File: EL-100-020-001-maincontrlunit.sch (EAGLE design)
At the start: 186 parts, among them T1 WS-TST-90°, U1 VNI4140K-32, U16 24AA256-I/SN, U19 ABS10-32.768KHZ-7-T, U2 VNI4140K-32, U3 VNI4140K-32, U8 MCP7940N-I/SN, U9 PMEG2005ET, X1 944-12-46-00, X10 S2L3.50/8/90G, X11 S2L3.50/8/90G, X12 S2L3.50/8/90G, X13 140-08-FLACHBAND1.27, X14 944-12-2-00, X2 944-12-46-00, X3 90G-14, X4 90G-14, X5 Q-063209, X6 Q-063209, X7 Q-063209, X8 Q-063209, X9 S2L3.50/8/90G

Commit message: extensions added
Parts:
- added C65: 1000pF, supply2:C1206C102KDRACTU
- C39, C40: value 4.7nF -> 4700pF
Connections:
- net AGND: now also C65.C1
- net PE: now also C65.C2
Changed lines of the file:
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@@
 </part>
 <part name="SUPPLY53" library="supply2" deviceset="PE" device=""/>
-<part name="C39" library="Kemet_By_element14_1" deviceset="C0805F472K1RACAUTO" device="" value="4.7nF"/>
-<part name="C40" library="Kemet_By_element14_1" deviceset="C0805F472K1RACAUTO" device="" value="4.7nF"/>
+<part name="C39" library="Kemet_By_element14_1" deviceset="C0805F472K1RACAUTO" device="" value="4700pF"/>
+<part name="C40" library="Kemet_By_element14_1" deviceset="C0805F472K1RACAUTO" device="" value="4700pF"/>
 <part name="SUPPLY54" library="supply2" deviceset="0V" device=""/>
 <part name="C1" library="Kemet_By_element14_1" deviceset="C1206C225K5RACTU" device="" value="2.2uF"/>
@@
 <attribute name="MF" value="VISHAY DRALORIC"/>
 </part>
+<part name="C65" library="supply2" deviceset="C1206C102KDRACTU" device="" value="1000pF">
+<attribute name="MF" value="KEMET"/>
+<attribute name="OC_FARNELL" value="1826304"/>
+</part>
+<part name="SUPPLY108" library="supply2" deviceset="AGND" device=""/>
+<part name="SUPPLY109" library="supply2" deviceset="PE" device=""/>
 </parts>
 <sheets>
@@
 <instance part="SUPPLY77" gate="PE" x="322.58" y="185.42"/>
 <instance part="SUPPLY79" gate="PE" x="322.58" y="208.28"/>
+<instance part="C65" gate="G$1" x="195.58" y="241.3" smashed="yes">
+<attribute name="VALUE" x="189.9158" y="237.0328" size="1.778" layer="96" ratio="10" rot="SR0"/>
+<attribute name="NAME" x="194.6656" y="244.0686" size="2.0828" layer="95" ratio="10" rot="SR0"/>
+<attribute name="MF" x="195.58" y="241.3" size="1.778" layer="96" rot="R270" display="off"/>
+</instance>
+<instance part="SUPPLY108" gate="G$1" x="182.88" y="236.22" rot="MR0"/>
+<instance part="SUPPLY109" gate="PE" x="213.36" y="236.22"/>
 </instances>
 <busses>
@@
 <pinref part="SUPPLY105" gate="G$1" pin="AGND"/>
 </segment>
+<segment>
+<pinref part="C65" gate="G$1" pin="C1"/>
+<pinref part="SUPPLY108" gate="G$1" pin="AGND"/>
+<wire x1="195.58" y1="241.3" x2="182.88" y2="241.3" width="0.1524" layer="91"/>
+<wire x1="182.88" y1="241.3" x2="182.88" y2="238.76" width="0.1524" layer="91"/>
+</segment>
 </net>
 <net name="ANA_1.1" class="0">
@@
 <pinref part="SUPPLY79" gate="PE" pin="PE"/>
 </segment>
+<segment>
+<pinref part="C65" gate="G$1" pin="C2"/>
+<pinref part="SUPPLY109" gate="PE" pin="PE"/>
+<wire x1="203.2" y1="241.3" x2="213.36" y2="241.3" width="0.1524" layer="91"/>
+<wire x1="213.36" y1="241.3" x2="213.36" y2="238.76" width="0.1524" layer="91"/>
+</segment>
 </net>

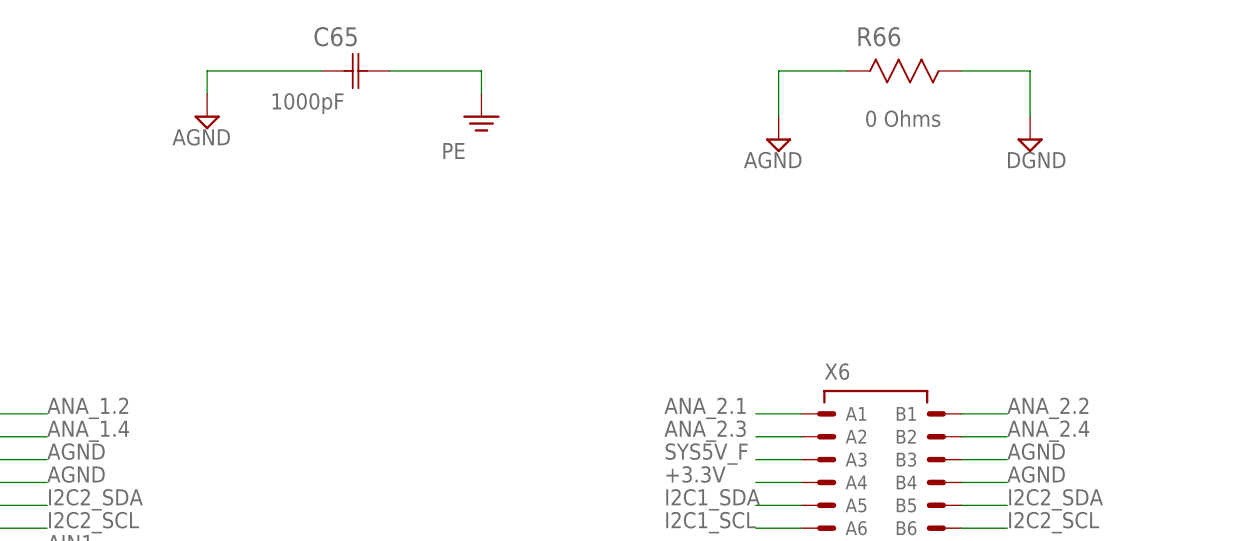
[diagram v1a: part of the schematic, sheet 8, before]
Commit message: DIN Rail extension
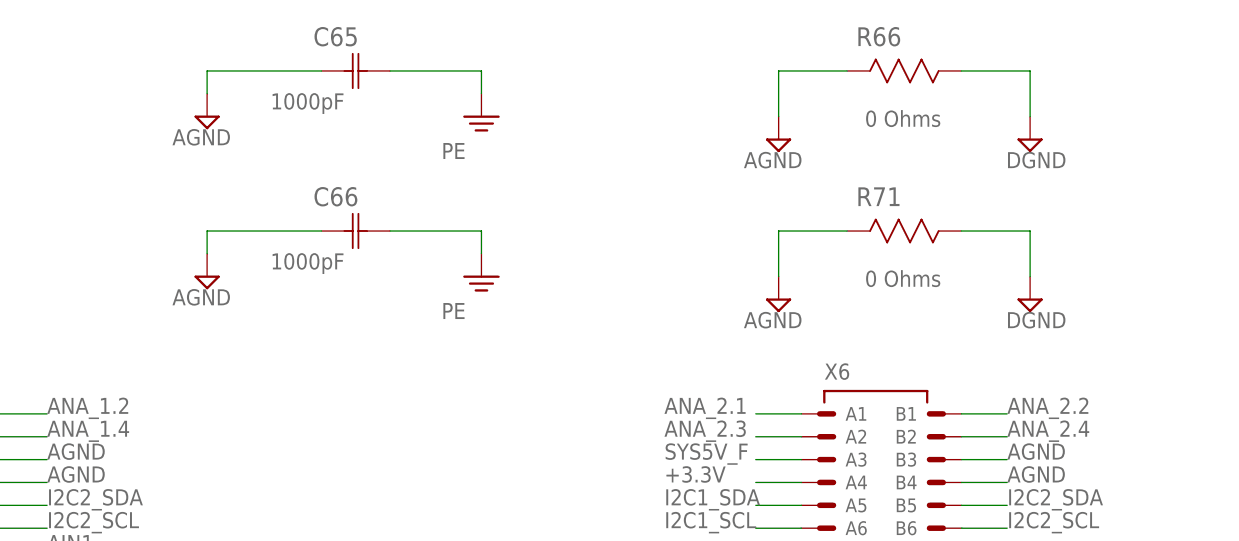
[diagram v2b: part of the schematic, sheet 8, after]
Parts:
- added C66: 1000pF, supply2:C1206C102KDRACTU
- added R71: 0 Ohms, Vishay_By_element14_Batch_1:CRCW12060000Z0EA
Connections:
- net AGND: now also C66.C1, R71.2
- net DGND: now also R71.1
- net PE: now also C66.C2
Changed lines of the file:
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@@
 <part name="SUPPLY108" library="supply2" deviceset="AGND" device=""/>
 <part name="SUPPLY109" library="supply2" deviceset="PE" device=""/>
+<part name="R71" library="Vishay_By_element14_Batch_1" deviceset="CRCW12060000Z0EA" device="" value="0 Ohms"/>
+<part name="SUPPLY110" library="supply2" deviceset="AGND" device=""/>
+<part name="SUPPLY111" library="supply2" deviceset="DGND" device=""/>
+<part name="C66" library="supply2" deviceset="C1206C102KDRACTU" device="" value="1000pF">
+<attribute name="MF" value="KEMET"/>
+<attribute name="OC_FARNELL" value="1826304"/>
+</part>
+<part name="SUPPLY112" library="supply2" deviceset="AGND" device=""/>
+<part name="SUPPLY113" library="supply2" deviceset="PE" device=""/>
 </parts>
 <sheets>
@@
 <instance part="SUPPLY108" gate="G$1" x="182.88" y="236.22" rot="MR0"/>
 <instance part="SUPPLY109" gate="PE" x="213.36" y="236.22"/>
+<instance part="R71" gate="A" x="254" y="223.52" smashed="yes">
+<attribute name="VALUE" x="255.9558" y="217.3224" size="1.778" layer="96" ratio="10" rot="SR0"/>
+<attribute name="NAME" x="254.9906" y="226.2886" size="2.0828" layer="95" ratio="10" rot="SR0"/>
+</instance>
+<instance part="SUPPLY110" gate="G$1" x="246.38" y="215.9" rot="MR0"/>
+<instance part="SUPPLY111" gate="G$1" x="274.32" y="215.9"/>
+<instance part="C66" gate="G$1" x="195.58" y="223.52" smashed="yes">
+<attribute name="VALUE" x="189.9158" y="219.2528" size="1.778" layer="96" ratio="10" rot="SR0"/>
+<attribute name="NAME" x="194.6656" y="226.2886" size="2.0828" layer="95" ratio="10" rot="SR0"/>
+<attribute name="MF" x="195.58" y="223.52" size="1.778" layer="96" rot="R270" display="off"/>
+</instance>
+<instance part="SUPPLY112" gate="G$1" x="182.88" y="218.44" rot="MR0"/>
+<instance part="SUPPLY113" gate="PE" x="213.36" y="218.44"/>
 </instances>
 <busses>
@@
 <wire x1="182.88" y1="241.3" x2="182.88" y2="238.76" width="0.1524" layer="91"/>
 </segment>
+<segment>
+<wire x1="254" y1="223.52" x2="246.38" y2="223.52" width="0.1524" layer="91"/>
+<wire x1="246.38" y1="223.52" x2="246.38" y2="218.44" width="0.1524" layer="91"/>
+<pinref part="R71" gate="A" pin="2"/>
+<pinref part="SUPPLY110" gate="G$1" pin="AGND"/>
+</segment>
+<segment>
+<pinref part="C66" gate="G$1" pin="C1"/>
+<pinref part="SUPPLY112" gate="G$1" pin="AGND"/>
+<wire x1="195.58" y1="223.52" x2="182.88" y2="223.52" width="0.1524" layer="91"/>
+<wire x1="182.88" y1="223.52" x2="182.88" y2="220.98" width="0.1524" layer="91"/>
+</segment>
 </net>
 <net name="ANA_1.1" class="0">
@@
 <wire x1="266.7" y1="241.3" x2="274.32" y2="241.3" width="0.1524" layer="91"/>
 </segment>
+<segment>
+<pinref part="SUPPLY111" gate="G$1" pin="DGND"/>
+<wire x1="274.32" y1="218.44" x2="274.32" y2="223.52" width="0.1524" layer="91"/>
+<pinref part="R71" gate="A" pin="1"/>
+<wire x1="266.7" y1="223.52" x2="274.32" y2="223.52" width="0.1524" layer="91"/>
+</segment>
 </net>
 <net name="PE" class="0">
@@
 <wire x1="213.36" y1="241.3" x2="213.36" y2="238.76" width="0.1524" layer="91"/>
 </segment>
+<segment>
+<pinref part="C66" gate="G$1" pin="C2"/>
+<pinref part="SUPPLY113" gate="PE" pin="PE"/>
+<wire x1="203.2" y1="223.52" x2="213.36" y2="223.52" width="0.1524" layer="91"/>
+<wire x1="213.36" y1="223.52" x2="213.36" y2="220.98" width="0.1524" layer="91"/>
+</segment>
 </net>
